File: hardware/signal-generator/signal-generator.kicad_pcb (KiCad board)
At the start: 2 copper layers, 100.1 x 100.1 mm, 63 parts, among them J1 AVR-ISP-6, J2 Conn_01x04_Male, J3 Power_Supply_Rails, J4 Conn_Coaxial, SW1 RESET_BUTTON, SW2 START/STOP, SW3 MODE_SELECT, SW4 UP_ARROW, SW5 DOWN_ARROW, SW6 Frequency_Step_Rotary_Encoder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

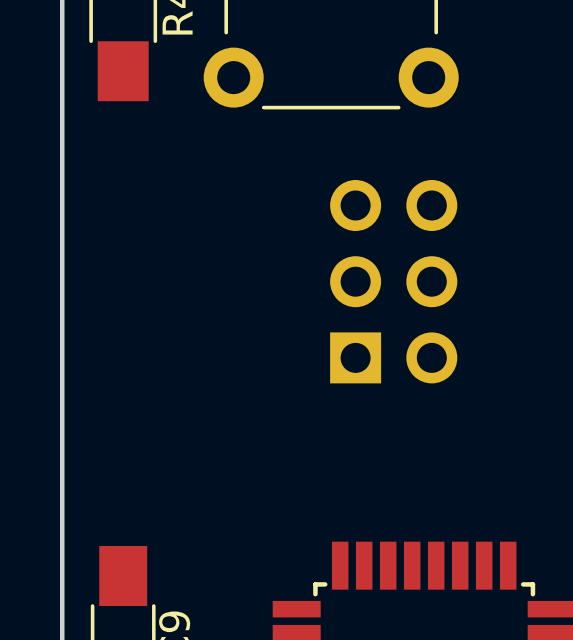
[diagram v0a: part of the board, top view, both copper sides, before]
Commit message: [Signal generator] Add 4 pin connector to ATMega328PB's port E
The additional connector is optional. The latter outsources the
microcontroller's port E which may be used for additional functionality.
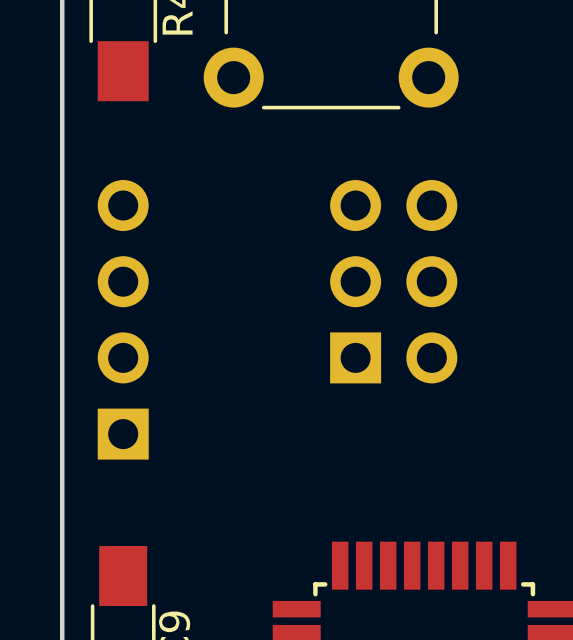
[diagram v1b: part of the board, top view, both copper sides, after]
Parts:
- added J5: Conn_01x04, Pin_Headers:Pin_Header_Straight_1x04_Pitch2.54mm, B.Cu at (110.1, 105.2)
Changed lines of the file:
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@@
     (tracks 0)
     (zones 0)
-    (modules 63)
+    (modules 64)
     (nets 59)
   )
@@
   (net 47 /DAC/SLEEP)
   (net 48 /DAC/CLK)
-  (net 49 "Net-(U1-Pad22)")
-  (net 50 "Net-(U1-Pad20)")
-  (net 51 "Net-(U1-Pad19)")
-  (net 52 /DAC/DB7)
-  (net 53 /DAC/DB6)
-  (net 54 /DAC/DB5)
-  (net 55 "Net-(U1-Pad6)")
-  (net 56 "Net-(U1-Pad3)")
-  (net 57 /DAC/DB4)
-  (net 58 /DAC/DB3)
+  (net 49 "Net-(U1-Pad20)")
+  (net 50 /DAC/DB7)
+  (net 51 /DAC/DB6)
+  (net 52 /DAC/DB5)
+  (net 53 /DAC/DB4)
+  (net 54 /DAC/DB3)
+  (net 55 "Net-(J5-Pad4)")
+  (net 56 "Net-(J5-Pad3)")
+  (net 57 "Net-(J5-Pad2)")
+  (net 58 "Net-(J5-Pad1)")
   (net_class Default "This is the default net class."
     (clearance 0.2)
@@
     (add_net "Net-(C12-Pad2)")
     (add_net "Net-(C18-Pad1)")
+    (add_net "Net-(J5-Pad1)")
+    (add_net "Net-(J5-Pad2)")
+    (add_net "Net-(J5-Pad3)")
+    (add_net "Net-(J5-Pad4)")
     (add_net "Net-(R10-Pad1)")
     (add_net "Net-(R11-Pad2)")
@@
     (add_net "Net-(SW6-PadS1)")
     (add_net "Net-(SW6-PadS2)")
-    (add_net "Net-(U1-Pad19)")
     (add_net "Net-(U1-Pad20)")
-    (add_net "Net-(U1-Pad22)")
-    (add_net "Net-(U1-Pad3)")
-    (add_net "Net-(U1-Pad6)")
   )
   (module Housings_QFP:TQFP-32_7x7mm_Pitch0.8mm (layer F.Cu)
@@
       (net 42 /FREQ_STEP_B))
     (pad 22 smd rect (at 4.25 -1.2 180) (size 1.6 0.55) (layers F.Cu F.Paste F.Mask)
-      (net 49 "Net-(U1-Pad22)"))
+      (net 55 "Net-(J5-Pad4)"))
     (pad 21 smd rect (at 4.25 -0.4 180) (size 1.6 0.55) (layers F.Cu F.Paste F.Mask)
       (net 1 AGND))
     (pad 20 smd rect (at 4.25 0.4 180) (size 1.6 0.55) (layers F.Cu F.Paste F.Mask)
-      (net 50 "Net-(U1-Pad20)"))
+      (net 49 "Net-(U1-Pad20)"))
     (pad 19 smd rect (at 4.25 1.2 180) (size 1.6 0.55) (layers F.Cu F.Paste F.Mask)
-      (net 51 "Net-(U1-Pad19)"))
+      (net 56 "Net-(J5-Pad3)"))
     (pad 18 smd rect (at 4.25 2 180) (size 1.6 0.55) (layers F.Cu F.Paste F.Mask)
       (net 8 +5VD))
@@
       (net 23 /BTN_ROW0))
     (pad 11 smd rect (at -1.2 4.25 270) (size 1.6 0.55) (layers F.Cu F.Paste F.Mask)
-      (net 52 /DAC/DB7))
+      (net 50 /DAC/DB7))
     (pad 10 smd rect (at -2 4.25 270) (size 1.6 0.55) (layers F.Cu F.Paste F.Mask)
-      (net 53 /DAC/DB6))
+      (net 51 /DAC/DB6))
     (pad 9 smd rect (at -2.8 4.25 270) (size 1.6 0.55) (layers F.Cu F.Paste F.Mask)
-      (net 54 /DAC/DB5))
+      (net 52 /DAC/DB5))
     (pad 8 smd rect (at -4.25 2.8 180) (size 1.6 0.55) (layers F.Cu F.Paste F.Mask)
       (net 5 /XTAL2))
@@
       (net 4 /XTAL1))
     (pad 6 smd rect (at -4.25 1.2 180) (size 1.6 0.55) (layers F.Cu F.Paste F.Mask)
-      (net 55 "Net-(U1-Pad6)"))
+      (net 57 "Net-(J5-Pad2)"))
     (pad 5 smd rect (at -4.25 0.4 180) (size 1.6 0.55) (layers F.Cu F.Paste F.Mask)
       (net 1 AGND))
@@
       (net 8 +5VD))
     (pad 3 smd rect (at -4.25 -1.2 180) (size 1.6 0.55) (layers F.Cu F.Paste F.Mask)
-      (net 56 "Net-(U1-Pad3)"))
+      (net 58 "Net-(J5-Pad1)"))
     (pad 2 smd rect (at -4.25 -2 180) (size 1.6 0.55) (layers F.Cu F.Paste F.Mask)
-      (net 57 /DAC/DB4))
+      (net 53 /DAC/DB4))
     (pad 1 smd rect (at -4.25 -2.8 180) (size 1.6 0.55) (layers F.Cu F.Paste F.Mask)
-      (net 58 /DAC/DB3))
+      (net 54 /DAC/DB3))
     (model ${KISYS3DMOD}/Housings_QFP.3dshapes/TQFP-32_7x7mm_Pitch0.8mm.wrl
       (at (xyz 0 0 0))
@@
       (net 44 /DAC/DB2))
     (pad 5 smd rect (at -4.7 -3.175) (size 2 0.6) (layers F.Cu F.Paste F.Mask)
-      (net 58 /DAC/DB3))
+      (net 54 /DAC/DB3))
     (pad 4 smd rect (at -4.7 -4.445) (size 2 0.6) (layers F.Cu F.Paste F.Mask)
-      (net 57 /DAC/DB4))
+      (net 53 /DAC/DB4))
     (pad 3 smd rect (at -4.7 -5.715) (size 2 0.6) (layers F.Cu F.Paste F.Mask)
-      (net 54 /DAC/DB5))
+      (net 52 /DAC/DB5))
     (pad 2 smd rect (at -4.7 -6.985) (size 2 0.6) (layers F.Cu F.Paste F.Mask)
-      (net 53 /DAC/DB6))
+      (net 51 /DAC/DB6))
     (pad 1 smd rect (at -4.7 -8.255) (size 2 0.6) (layers F.Cu F.Paste F.Mask)
-      (net 52 /DAC/DB7))
+      (net 50 /DAC/DB7))
     (model ${KISYS3DMOD}/Housings_SOIC.3dshapes/SOIC-28W_7.5x17.9mm_Pitch1.27mm.wrl
       (at (xyz 0 0 0))
@@
       (at (xyz 0 0 0))
       (scale (xyz 1 1 1))
+      (rotate (xyz 0 0 0))
+    )
+  )
+  (module Pin_Headers:Pin_Header_Straight_1x04_Pitch2.54mm (layer B.Cu)
+    (at 110.109 105.156)
+    (descr "Through hole straight pin header, 1x04, 2.54mm pitch, single row")
+    (tags "Through hole pin header THT 1x04 2.54mm single row")
+    (fp_text reference J5 (at 0 2.33) (layer B.SilkS)
+      (effects (font (size 1 1) (thickness 0.15)) (justify mirror))
+    )
+    (fp_text value Conn_01x04 (at 0 -9.95) (layer B.Fab)
+      (effects (font (size 1 1) (thickness 0.15)) (justify mirror))
+    )
+    (fp_text user %R (at 0 -3.81 -90) (layer B.Fab)
+      (effects (font (size 1 1) (thickness 0.15)) (justify mirror))
+    )
+    (fp_line (start 1.8 1.8) (end -1.8 1.8) (layer B.CrtYd) (width 0.05))
+    (fp_line (start 1.8 -9.4) (end 1.8 1.8) (layer B.CrtYd) (width 0.05))
+    (fp_line (start -1.8 -9.4) (end 1.8 -9.4) (layer B.CrtYd) (width 0.05))
+    (fp_line (start -1.8 1.8) (end -1.8 -9.4) (layer B.CrtYd) (width 0.05))
+    (fp_line (start -1.33 1.33) (end 0 1.33) (layer B.SilkS) (width 0.12))
+    (fp_line (start -1.33 0) (end -1.33 1.33) (layer B.SilkS) (width 0.12))
+    (fp_line (start -1.33 -1.27) (end 1.33 -1.27) (layer B.SilkS) (width 0.12))
+    (fp_line (start 1.33 -1.27) (end 1.33 -8.95) (layer B.SilkS) (width 0.12))
+    (fp_line (start -1.33 -1.27) (end -1.33 -8.95) (layer B.SilkS) (width 0.12))
+    (fp_line (start -1.33 -8.95) (end 1.33 -8.95) (layer B.SilkS) (width 0.12))
+    (fp_line (start -1.27 0.635) (end -0.635 1.27) (layer B.Fab) (width 0.1))
+    (fp_line (start -1.27 -8.89) (end -1.27 0.635) (layer B.Fab) (width 0.1))
+    (fp_line (start 1.27 -8.89) (end -1.27 -8.89) (layer B.Fab) (width 0.1))
+    (fp_line (start 1.27 1.27) (end 1.27 -8.89) (layer B.Fab) (width 0.1))
+    (fp_line (start -0.635 1.27) (end 1.27 1.27) (layer B.Fab) (width 0.1))
+    (pad 4 thru_hole oval (at 0 -7.62) (size 1.7 1.7) (drill 1) (layers *.Cu *.Mask)
+      (net 55 "Net-(J5-Pad4)"))
+    (pad 3 thru_hole oval (at 0 -5.08) (size 1.7 1.7) (drill 1) (layers *.Cu *.Mask)
+      (net 56 "Net-(J5-Pad3)"))
+    (pad 2 thru_hole oval (at 0 -2.54) (size 1.7 1.7) (drill 1) (layers *.Cu *.Mask)
+      (net 57 "Net-(J5-Pad2)"))
+    (pad 1 thru_hole rect (at 0 0) (size 1.7 1.7) (drill 1) (layers *.Cu *.Mask)
+      (net 58 "Net-(J5-Pad1)"))
+    (model ${KISYS3DMOD}/Pin_Headers.3dshapes/Pin_Header_Straight_1x04_Pitch2.54mm.wrl
+      (at (xyz 0 0 0))
+      (scale (xyz 1 1 1))

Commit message: [Signal generator] Assign 3D models to components
Not all components have had a 3D model associated with them because I
have chosen to use 3D models only from KiCad's official GitHub
repository.
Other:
- net class Default: clearance 0.2 -> 0.15; via_dia 0.8 -> 0.6; via_drill 0.4 -> 0.3
- net class Digital Signal added: clearance 0.15, trace_width 0.15, via_dia 0.6, via_drill 0.3
- rule trace_clearance: 0.2 -> 0.15
- rule trace_min: 0.2 -> 0.127
- rule via_min_size: 0.4 -> 0.6

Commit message: [Signal generator] Route components no PCB
This is not the final routing of the PCB. Further optimization is
required. Moreover, the ground planes have not been placed.
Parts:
- C1, C19, C2, C20, C5, C6, C7: moved to F.Cu
- J3: footprint Pin_Headers:Pin_Header_Straight_2x04_Pitch2.54mm -> Pin_Headers:Pin_Header_Straight_2x05_Pitch2.54mm
- R18: moved to B.Cu
- moved J5 7.62 mm to (110.1, 97.5), turned to 180 degrees
- moved C5 7.52 mm to (158.8, 88.8)
- moved C6 7.52 mm to (158.8, 70.5)
- moved C7 7.31 mm to (142.9, 87.0), turned to 270 degrees
- moved C10 6.94 mm to (156.7, 110.0)
- moved R18 6.41 mm to (186.6, 120.5)
- moved C18 5.95 mm to (182.1, 107.1)
- moved R13 5.91 mm to (193.4, 116.0)
- moved R14 5.91 mm to (193.4, 109.0)
- moved RV4 5.91 mm to (197.6, 109.9)
- moved C11 5.55 mm to (156.7, 119.6)
- moved C12 5.55 mm to (156.7, 115.1)
- moved R5 5.55 mm to (156.7, 117.3)
- moved C20 5.30 mm to (186.6, 105.0)
- moved R19 5.30 mm to (185.8, 112.3)
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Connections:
- J1 pad 4: /BTN_COL1 -> /BTN_COL0
- J3 pad 7: +5VD -> AGND
- U1 pad 12: /BTN_ROW0 -> /BTN_ROW1
- U1 pad 13: /BTN_ROW1 -> /BTN_ROW0
- U1 pad 14: /BTN_COL0 -> /BTN_COL1
- U1 pad 15: /BTN_COL1 -> /BTN_COL0
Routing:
- net /FREQ_STEP_B: track 0.00 -> 189.8 mm, vias 0 -> 2
- net /FREQ_STEP_A: track 0.00 -> 181.9 mm, vias 0 -> 2
- net +5VD: track 0.00 -> 150.6 mm, vias 0 -> 2
- net +5VA: track 0.00 -> 117.5 mm, vias 0 -> 3
- net -5VA: track 0.00 -> 110.6 mm, vias 0 -> 1
- net -12VA: track 0.00 -> 84.5 mm, vias 0 -> 2
- net /BTN_COL0: track 0.00 -> 72.5 mm, vias 0 -> 5
- net /BTN_COL1: track 0.00 -> 63.3 mm, vias 0 -> 2
- net +12VA: track 0.00 -> 62.9 mm, vias 0 -> 2
- net Net-(R10-Pad1): track 0.00 -> 61.6 mm, vias 0 -> 1
- net /DAC/CLK: track 0.00 -> 58.8 mm, vias 0 -> 4
- net /~RESET: track 0.00 -> 57.2 mm, vias 0 -> 5
- net /BTN_ROW0: track 0.00 -> 54.2 mm, vias 0 -> 4
- net Net-(R15-Pad2): track 0.00 -> 46.5 mm, vias 0 -> 2
- net /BTN_ROW1: track 0.00 -> 43.7 mm, vias 0 -> 4
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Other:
- net class Analog Signal added: clearance 0.15, trace_width 0.25, via_dia 0.6, via_drill 0.3
- net class Analog Supply added: clearance 0.15, trace_width 0.5, via_dia 0.8, via_drill 0.4
- net class Digital Supply added: clearance 0.15, trace_width 0.25, via_dia 0.6, via_drill 0.3

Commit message: [Signal generator] Finalize PCB layout
The presented board design is final for rev. 1. Here is a list of
changes introduced since the last commit:
  - The power supply's connector has been changed from a 10-pin
  one to a 12-pin. The additional 2 pins are not connected(NC). The
  reasoning behind this change is that the 2 pins increase the space
  between the analog and digital supply rails, therefore allowing both
  ground planes to be properly separated.
  - Add digital and analog ground planes, which are connected at a star
  point (Note: both planes are displayed as one(AGND) on the board.
  This is a consequence of the direct connection of both grounds on the
  schematic sheet).
  - Optimize layout and routing.
  - Include mounting holes.
  - Resize board to fit layout of components (board dimensions are
  included on the "F.Fab" layer).
  - Realign references and other text on the "Silk" and "Fab" layers.
  - Set page settings of PCB.
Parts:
- added REF**: MountingHole_3mm, Mounting_Holes:MountingHole_3mm, F.Cu at (114.7, 64.9)
- added REF**: MountingHole_3mm, Mounting_Holes:MountingHole_3mm, F.Cu at (194.2, 147.6)
- added REF**: MountingHole_3mm, Mounting_Holes:MountingHole_3mm, F.Cu at (114.8, 147.7)
- added REF**: MountingHole_3mm, Mounting_Holes:MountingHole_3mm, F.Cu at (194.1, 64.9)
- J3: footprint Pin_Headers:Pin_Header_Straight_2x05_Pitch2.54mm -> Pin_Headers:Pin_Header_Straight_2x06_Pitch2.54mm
- moved J4 2.99 mm to (194.2, 133.9)
- moved C1 2.54 mm to (153.0, 87.0)
- moved C2 2.54 mm to (153.0, 72.3)
- moved J3 2.54 mm to (155.6, 80.9)
- moved SW6 1.27 mm to (190.9, 81.5)
- moved C13 0.89 mm to (163.3, 112.5)
- moved C24 0.51 mm to (156.0, 104.8)
- moved C10 0.36 mm to (156.5, 110.2)
- moved D1 0.25 mm to (114.8, 126.1)
- moved C9 0.25 mm to (112.0, 113.8)
- moved R1 0.22 mm to (114.8, 128.8)
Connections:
- J3 pad 7: AGND -> Net-(J3-Pad7)
- J3 pad 8: AGND -> Net-(J3-Pad8)
- J3 pad 9: +5VD -> AGND
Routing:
- net AGND: track 3.34 -> 52.4 mm, vias 2 -> 26
- net +5VA: track 117.5 -> 135.5 mm
- net /FREQ_STEP_A: track 181.9 -> 166.4 mm, vias 2 -> 4
- net Net-(J5-Pad3): track 14.7 -> 29.1 mm
- net /FREQ_STEP_B: track 189.8 -> 176.2 mm, vias 2 -> 4
- net Net-(J5-Pad4): track 14.1 -> 24.0 mm
- net /~RESET: track 57.2 -> 49.9 mm, vias 5 -> 2
- net Net-(C10-Pad2): track 0.00 -> 3.44 mm
- net -5VA: track 110.6 -> 108.1 mm
- net -12VA: track 84.5 -> 82.2 mm
- net +12VA: track 62.9 -> 60.6 mm
- net /Output_Circuitry/VOUT: track 38.6 -> 36.7 mm
- net /Output_Circuitry/IINB: track 19.3 -> 18.0 mm, vias 0 -> 2
- net /Output_Circuitry/IINA: track 19.3 -> 18.0 mm, vias 0 -> 2
- net /BTN_ROW1: track 43.7 -> 42.5 mm, vias 4 -> 3
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- added copper zone on B.Cu, net AGND
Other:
- board size 100.1 x 100.1 mm -> 96.6 x 92.2 mm
- board text added: "+12VA"
- board text added: "+5VA"
- board text added: "+5VD"
- board text added: "-12VA"
- board text added: "-5VA"
- board text added: "AGND"
- board text added: "AGND PLANE"
- board text added: "BALANCE"
- board text added: "COARSE"
- board text added: "DESIGNED BY: PETAR NIKOLOV"
- board text added: "DGND"
- board text added: "DGND PLANE"
- board text added: "DIGITAL FUNCTION GENERATOR"
- board text added: "FINE"
- board text added: "FREQUENCY STEP"
- board text added: "GND"
- board text added: "LCD"
- board text added: "NC"
- board text added: "OFFSET"
- board text added: "OUT 50Ω"
- board text added: "PORT E"
- board text added: "RESET"
